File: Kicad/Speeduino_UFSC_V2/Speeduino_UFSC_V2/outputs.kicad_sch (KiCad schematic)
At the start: 16 parts, among them J3 Conn_01x06, Q2 Q_NMOS_GDSD, Q3 HVM NMOS, U5 ULN2003

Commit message: Add pdf
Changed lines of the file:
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@@
 	(wire
 		(pts
+			(xy 57.15 73.66) (xy 66.04 73.66)
+		)
+		(stroke
+			(width 0)
+			(type default)
+		)
+	)
+	(wire
+		(pts
 			(xy 189.23 48.26) (xy 196.85 48.26)
 		)
@@
 	(wire
 		(pts
+			(xy 57.15 71.12) (xy 66.04 71.12)
+		)
+		(stroke
+			(width 0)
+			(type default)
+		)
+	)
+	(wire
+		(pts
 			(xy 214.63 33.02) (xy 223.52 33.02)
 		)
@@
 	(wire
 		(pts
+			(xy 57.15 68.58) (xy 66.04 68.58)
+		)
+		(stroke
+			(width 0)
+			(type default)
+		)
+	)
+	(wire
+		(pts
 			(xy 196.85 48.26) (xy 196.85 46.99)
 		)
@@
 	(global_label "MCU-D49"
 		(shape input)
-		(at 66.04 73.66 180)
+		(at 57.15 73.66 180)
 		(effects
 			(font
@@
 		)
 		(property "Intersheetrefs" "${INTERSHEET_REFS}"
-			(at 66.04 73.66 0)
+			(at 57.15 73.66 0)
 			(effects
 				(font
@@
 	(global_label "MCU-D45"
 		(shape input)
-		(at 66.04 71.12 180)
+		(at 57.15 71.12 180)
 		(effects
 			(font
@@
 		)
 		(property "Intersheetrefs" "${INTERSHEET_REFS}"
-			(at 66.04 71.12 0)
+			(at 57.15 71.12 0)
 			(effects
 				(font
@@
 	(global_label "MCU-D47"
 		(shape input)
-		(at 66.04 68.58 180)
+		(at 57.15 68.58 180)
 		(effects
 			(font
@@
 		)
 		(property "Intersheetrefs" "${INTERSHEET_REFS}"
-			(at 66.04 68.58 0)
+			(at 57.15 68.58 0)
 			(effects
 				(font
@@
 			)
 		)
-		(property "Description" ""
+		(property "Description" "Resistor"
 			(at 64.77 144.78 0)
 			(effects
@@
 			)
 		)
-		(property "Description" ""
+		(property "Description" "Power symbol creates a global label with name \"GND\" , ground"
 			(at 214.63 46.99 0)
 			(effects
@@
 			)
 		)
-		(property "Description" ""
+		(property "Description" "N-MOSFET transistor, drain/gate/source"
 			(at 212.09 63.5 0)
 			(effects
@@
 			)
 		)
-		(property "Description" ""
+		(property "Description" "Resistor"
 			(at 207.01 68.58 0)
 			(effects
@@
 			)
 		)
-		(property "Description" ""
+		(property "Description" "Diode"
 			(at 227.33 38.1 0)
 			(effects
@@
 			)
 		)
+		(property "Sim.Device" "D"
+			(at 227.33 38.1 0)
+			(effects
+				(font
+					(size 1.27 1.27)
+				)
+				(hide yes)
+			)
+		)
+		(property "Sim.Pins" "1=K 2=A"
+			(at 227.33 38.1 0)
+			(effects
+				(font
+					(size 1.27 1.27)
+				)
+				(hide yes)
+			)
+		)
 		(pin "1"
 		)
@@
 			)
 		)
-		(property "Description" ""
+		(property "Description" "High Voltage, High Current Darlington Transistor Arrays, SOIC16/SOIC16W/DIP16/TSSOP16"
 			(at 76.2 63.5 0)
 			(effects
@@
 			)
 		)
-		(property "Description" ""
+		(property "Description" "Resistor"
 			(at 88.9 78.74 0)
 			(effects
@@
 			)
 		)
-		(property "Description" ""
+		(property "Description" "Power symbol creates a global label with name \"GND\" , ground"
 			(at 66.04 156.21 0)
 			(effects
@@
 			)
 		)
-		(property "Description" ""
+		(property "Description" "Power symbol creates a global label with name \"GND\" , ground"
 			(at 227.33 149.86 0)
 			(effects
@@
 			)
 		)
-		(property "Description" ""
+		(property "Description" "Resistor"
 			(at 196.85 68.58 0)
 			(effects
@@
 			)
 		)
-		(property "Description" ""
+		(property "Description" "Power symbol creates a global label with name \"GND\" , ground"
 			(at 45.72 52.07 0)
 			(effects
@@
 			)
 		)
-		(property "Description" ""
+		(property "Description" "Resistor"
 			(at 196.85 43.18 0)
 			(effects
@@
 			)
 		)
-		(property "Description" ""
+		(property "Description" "Resistor"
 			(at 207.01 43.18 0)
 			(effects
@@
 			)
 		)
-		(property "Description" ""
+		(property "Description" "Diode"
 			(at 227.33 63.5 0)
 			(effects
@@
 			)
 		)
+		(property "Sim.Device" "D"
+			(at 227.33 63.5 0)
+			(effects
+				(font
+					(size 1.27 1.27)
+				)
+				(hide yes)
+			)
+		)
+		(property "Sim.Pins" "1=K 2=A"
+			(at 227.33 63.5 0)
+			(effects
+				(font
+					(size 1.27 1.27)
+				)
+				(hide yes)
+			)
+		)
 		(pin "1"
 		)
@@
 			)
 		)
-		(property "Description" ""
+		(property "Description" "Power symbol creates a global label with name \"GND\" , ground"
 			(at 196.85 63.5 0)
 			(effects
@@
 			)
 		)
-		(property "Description" ""
+		(property "Description" "Resistor"
 			(at 57.15 54.61 0)
 			(effects
@@
 			)
 		)
-		(property "Description" ""
+		(property "Description" "Power symbol creates a global label with name \"GND\" , ground"
 			(at 214.63 72.39 0)
 			(effects
@@
 			)
 		)
-		(property "Description" ""
+		(property "Description" "Pololu Breakout Board, Stepper Driver DRV8825"
 			(at 219.71 127 0)
 			(effects
@@
 			)
 		)
-		(property "Description" ""
+		(property "Description" "Resistor"
 			(at 71.12 151.13 0)
 			(effects
@@
 			)
 		)
-		(property "Description" ""
+		(property "Description" "Power symbol creates a global label with name \"GND\" , ground"
 			(at 64.77 138.43 0)
 			(effects
@@
 			)
 		)
-		(property "Description" ""
+		(property "Description" "Resistor"
 			(at 57.15 60.96 0)
 			(effects
@@
 			)
 		)
-		(property "Description" ""
+		(property "Description" "N-MOSFET transistor, drain/gate/source"
 			(at 212.09 38.1 0)
 			(effects
@@
 			)
 		)
-		(property "Description" ""
+		(property "Description" "Power symbol creates a global label with name \"GND\" , ground"
 			(at 196.85 38.1 0)
 			(effects
@@
 			)
 		)
-		(property "Description" ""
+		(property "Description" "Generic connector, single row, 01x06, script generated (kicad-library-utils/schlib/autogen/connector/)"
 			(at 55.88 156.21 0)
 			(effects
@@
 			)
 		)
-		(property "Description" ""
+		(property "Description" "Power symbol creates a global label with name \"GND\" , ground"
 			(at 76.2 78.74 0)
 			(effects

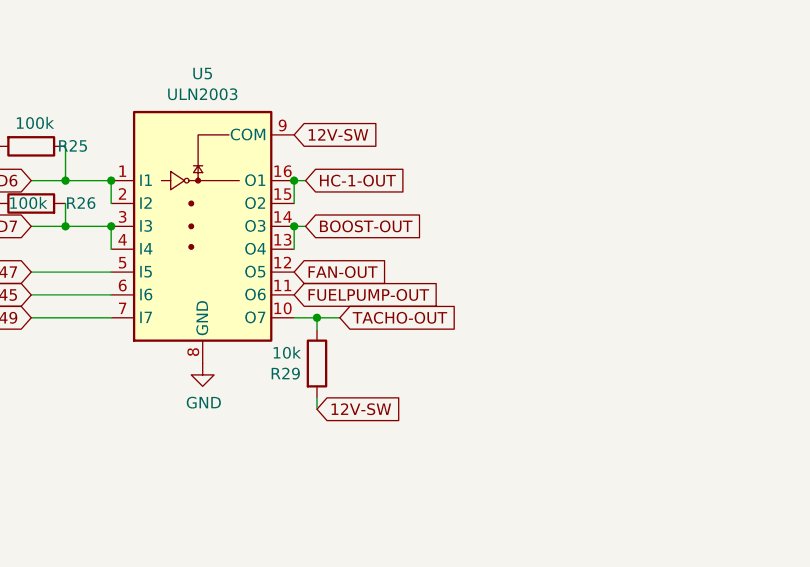
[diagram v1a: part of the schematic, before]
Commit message: Add 2 injectors in schematic
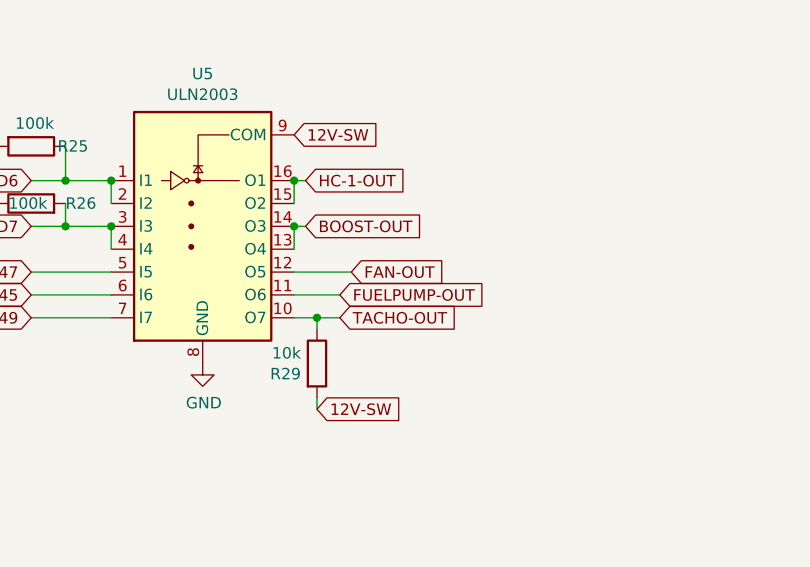
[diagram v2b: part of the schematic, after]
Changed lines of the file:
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@@
+	(wire
+		(pts
+			(xy 91.44 71.12) (xy 86.36 71.12)
+		)
+		(stroke
+			(width 0)
+			(type default)
+		)
+	)
 	(wire
 		(pts
@@
 		(pts
 			(xy 57.15 63.5) (xy 60.96 63.5)
+		)
+		(stroke
+			(width 0)
+			(type default)
+		)
+	)
+	(wire
+		(pts
+			(xy 92.71 68.58) (xy 86.36 68.58)
 		)
 		(stroke
@@
 	(global_label "FAN-OUT"
 		(shape input)
-		(at 86.36 68.58 0)
+		(at 92.71 68.58 0)
 		(effects
 			(font
@@
 		)
 		(property "Intersheetrefs" "${INTERSHEET_REFS}"
-			(at 86.36 68.58 0)
+			(at 92.71 68.58 0)
 			(effects
 				(font
@@
 	(global_label "FUELPUMP-OUT"
 		(shape input)
-		(at 86.36 71.12 0)
+		(at 91.44 71.12 0)
 		(effects
 			(font
@@
 		)
 		(property "Intersheetrefs" "${INTERSHEET_REFS}"
-			(at 86.36 71.12 0)
-			(effects
-				(font
+			(at 91.44 71.12 0)
+			(effects
+				(font
